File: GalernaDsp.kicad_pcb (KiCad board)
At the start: 4 copper layers, 121 x 121 mm, 124 parts, among them CN100 HX JN1.27-2X5 TP H4.9, J100 DM3CS-SF, J200 Headphones, J201 AudioInput, J202 AudioOutput, J300 USB_C_Receptacle_USB2.0_16P, SW400 100SP1T1B4M2QE, SW401 100SP1T1B4M2QE, U100 SW_RUN, U101 STM32F405RGTx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

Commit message: routing update
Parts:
- C116: footprint Capacitor_SMD:C_0402_1005Metric -> Capacitor_SMD:C_0603_1608Metric
- L100: footprint Inductor_SMD:L_0603_1608Metric -> Inductor_SMD:L_0402_1005Metric
- L300: footprint Inductor_SMD:L_0805_2012Metric -> Inductor_SMD:L_Sunlord_MWSA0618S
- moved R208 36.5 mm to (221.3, 88.4), turned to -90 degrees
- moved R209 35.0 mm to (218.9, 88.4), turned to -90 degrees
- moved C214 32.7 mm to (222.6, 92.5), turned to -90 degrees
- moved R206 32.1 mm to (220.8, 91.7), turned to 90 degrees
- moved R207 31.3 mm to (219.6, 91.7), turned to 90 degrees
- moved C215 29.1 mm to (217.8, 92.5), turned to -90 degrees
- moved FB100 19.1 mm to (223.5, 44.0)
- moved C208 17.9 mm to (201.1, 86.0), turned to 180 degrees
- moved C206 15.8 mm to (201.7, 87.4), turned to 180 degrees
- moved C201 14.8 mm to (211.7, 87.5), turned to 0 degrees
- moved D300 13.7 mm to (234.5, 59.6)
- moved C115 13.7 mm to (223.0, 48.6)
- moved C203 13.2 mm to (205.4, 87.4), turned to 180 degrees
- moved R304 10.7 mm to (234.5, 60.9), turned to 180 degrees
- moved R210 9.41 mm to (224.0, 100.9), turned to 90 degrees
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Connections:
- net /[1] MCU/SWDCLK renamed /[1] MCU/SWD_CLK
- net /[1] MCU/SWDIO renamed /[1] MCU/SWD_IO
- net /[1] MCU/SWO renamed /[1] MCU/SWD_O
- net Net-(U101-VDDA) renamed /[1] MCU/VDDA
- J300 pad S1: GND -> unconnected-(J300-SHIELD-PadS1)_2
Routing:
- net /[1] MCU/OLED_SPI_DATA: track 0.00 -> 104.7 mm
- net /[1] MCU/OLED_SPI_SCK: track 0.00 -> 80.2 mm
- net /[1] MCU/OLED_DC: track 0.00 -> 76.7 mm, vias 0 -> 2
- net /[1] MCU/OLED_RST: track 0.00 -> 72.2 mm, vias 0 -> 2
- net /[1] MCU/OLED_SPI_CS: track 0.00 -> 61.0 mm
- net GND: track 2.08 -> 49.1 mm, vias 0 -> 49
- net /[1] MCU/MCU_NRST: track 0.00 -> 41.3 mm, vias 0 -> 2
- net CODEC_I2S_MCK: track 0.00 -> 35.5 mm
- net CODEC_I2S_SDI: track 0.00 -> 32.5 mm, vias 0 -> 2
- net CODEC_I2C_SCL: track 0.00 -> 29.2 mm, vias 0 -> 2
- net MCU_USB_D-: track 0.00 -> 27.6 mm
- net MCU_USB_D+: track 0.00 -> 27.6 mm
- net CODEC_I2S_SD: track 0.00 -> 27.3 mm
- net CODEC_I2C_SDA: track 0.00 -> 26.5 mm
- net /[1] MCU/SWD_IO: track 0.00 -> 25.2 mm
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- added copper zone on F.Cu, net +3V3A
- added copper zone on F.Cu, net /[1] MCU/VDDA
- added copper zone on F.Cu, net /[2] Power/BUCK_SW
- added copper zone on F.Cu, net VBUS
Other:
- board text added: "PWR_ON"

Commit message: last updates
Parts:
- moved C115 8.18 mm to (231.2, 48.5), turned to 180 degrees
- moved FB100 7.74 mm to (221.6, 36.5)
- moved R105 6.78 mm to (206.1, 54.6)
- moved C113 5.69 mm to (213.7, 35.5)
- moved C111 3.00 mm to (213.8, 36.9)
- moved R110 2.43 mm to (175.8, 87.9)
- moved R112 2.40 mm to (181.5, 87.9)
- moved D101 2.40 mm to (175.8, 91.3)
- moved D102 2.38 mm to (178.6, 91.3)
- moved D103 2.38 mm to (181.5, 91.3)
- moved R111 2.34 mm to (178.6, 87.9)
- moved R109 1.89 mm to (211.4, 54.6)
- moved D104 1.78 mm to (210.9, 36.2)
- moved R106 1.55 mm to (214.4, 54.6)
- moved R108 1.55 mm to (208.3, 54.6)
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- renumbered CN100 to SWD
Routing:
- net Net-(J100-CLK): track 0.00 -> 31.3 mm
- net /[1] MCU/SDCARD_SDIO_D0: track 0.00 -> 28.6 mm, vias 0 -> 2
- net /[1] MCU/SDCARD_SDIO_D1: track 0.00 -> 25.9 mm, vias 0 -> 2
- net /[1] MCU/SDCARD_SDIO_D3: track 0.00 -> 21.6 mm
- net /[1] MCU/SDCARD_DETECT: track 0.00 -> 18.7 mm
- net /[1] MCU/SDCARD_SDIO_CMD: track 0.00 -> 17.9 mm, vias 0 -> 2
- net /[1] MCU/SDCARD_SDIO_D2: track 0.00 -> 15.8 mm
- net /[1] MCU/MCU_NRST: track 41.3 -> 35.2 mm
- net /[1] MCU/SDCARD_SDIO_CK: track 0.00 -> 2.54 mm
- net /[1] MCU/SWD_CLK: track 12.5 -> 14.1 mm, vias 0 -> 2
- net /[1] MCU/SWD_IO: track 25.2 -> 25.1 mm, vias 0 -> 2
- net GND: vias 49 -> 59

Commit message: updated placement
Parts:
- moved FB100 12.0 mm to (230.0, 45.0)
- moved C115 7.41 mm to (234.2, 55.3)
- moved D104 2.77 mm to (213.6, 36.8)
- moved C113 2.73 mm to (211.0, 35.4)
- moved C111 2.21 mm to (211.6, 36.8)
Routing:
- net /[1] MCU/SDCARD_SDIO_CMD: track 17.9 -> 37.6 mm, vias 2 -> 4
- net /[1] MCU/SDCARD_SDIO_D2: track 15.8 -> 31.8 mm, vias 0 -> 2
- net /[1] MCU/SDCARD_SDIO_D3: track 21.6 -> 37.5 mm, vias 0 -> 2
- net /[1] MCU/SDCARD_SDIO_D1: track 25.9 -> 41.8 mm
- net /[1] MCU/SDCARD_SDIO_D0: track 28.6 -> 44.3 mm, vias 2 -> 4
- net Net-(J100-CLK): track 31.3 -> 33.9 mm, vias 0 -> 2
- net GND: track 49.1 -> 50.7 mm, vias 59 -> 74
- added copper zone on F.Cu, net /[1] MCU/+3V3_SD

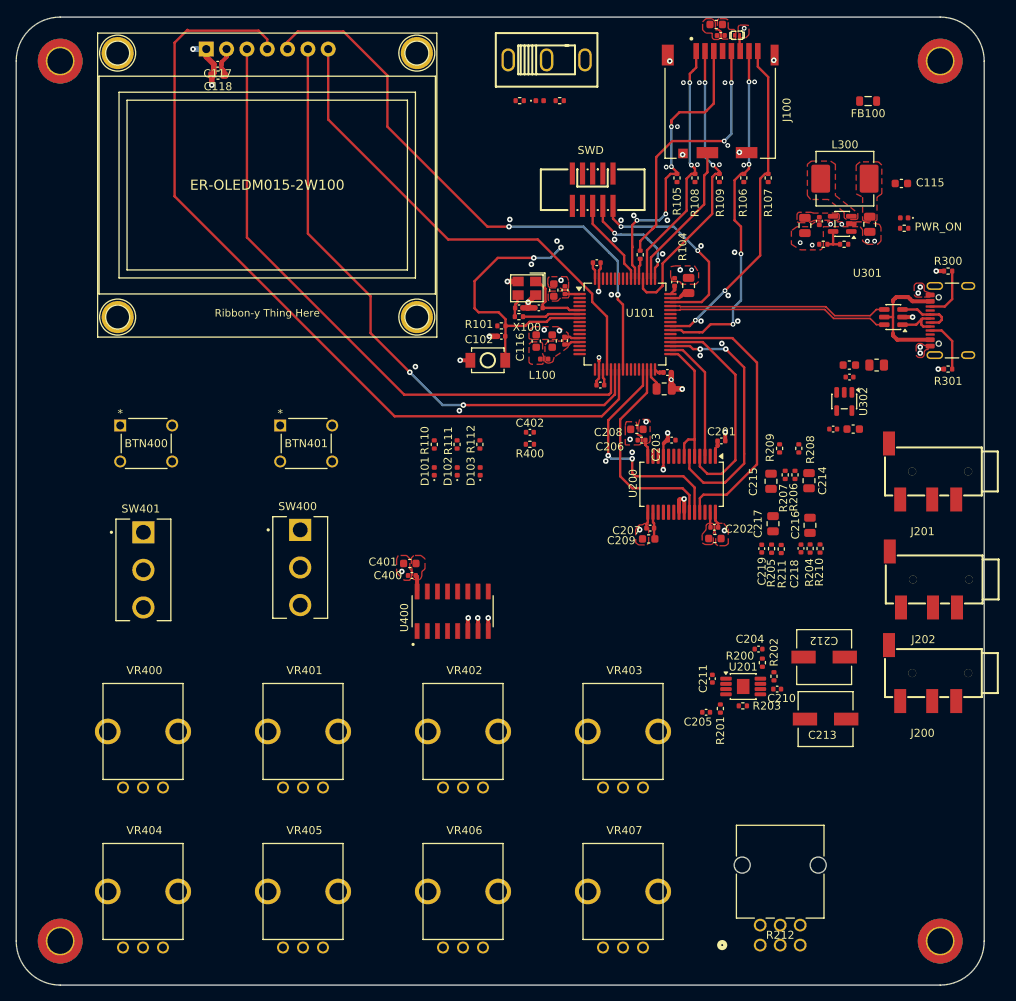
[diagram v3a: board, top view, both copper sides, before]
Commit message: headphone amplifier routing
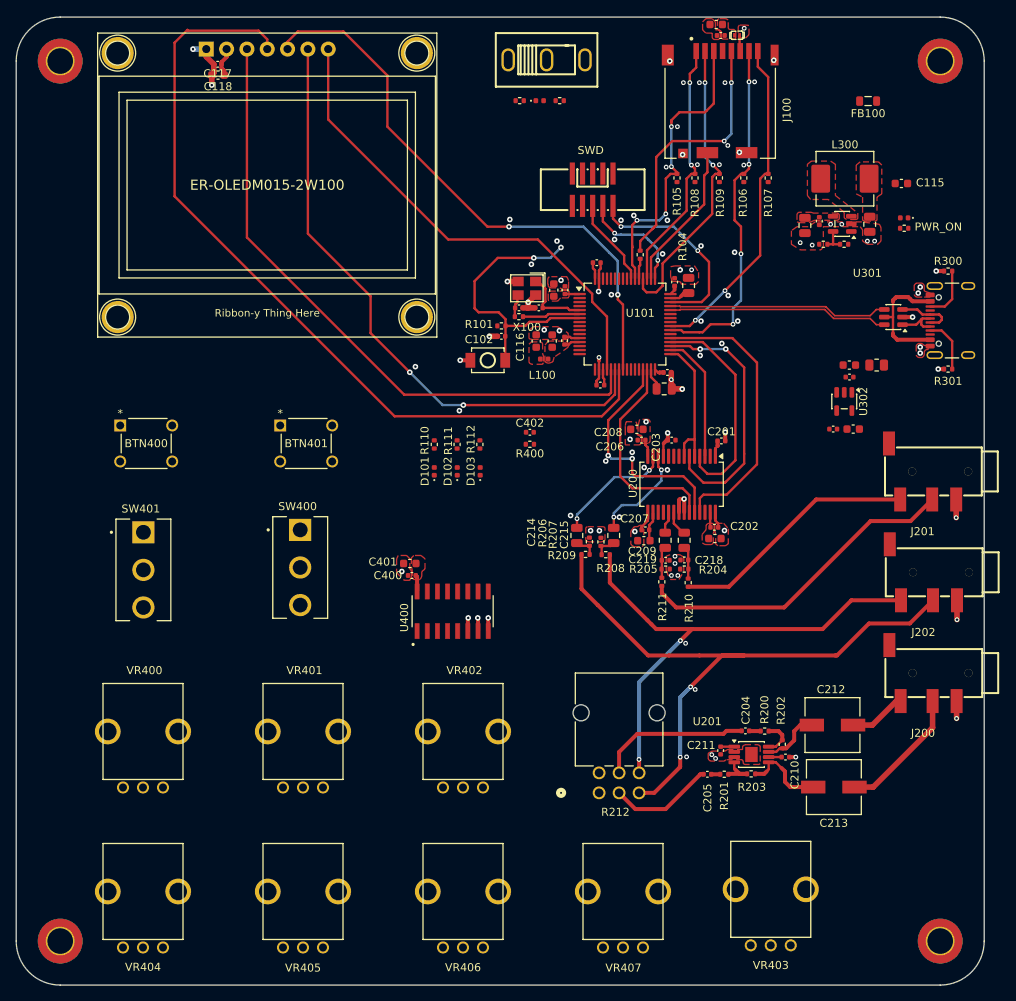
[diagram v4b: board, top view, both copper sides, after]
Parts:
- moved R212 27.7 mm to (196.4, 131.5)
- moved R209 27.6 mm to (194.7, 101.7), turned to 180 degrees
- moved R208 27.5 mm to (197.2, 101.7), turned to 0 degrees
- moved VR403 27.0 mm to (217.8, 150.5)
- moved R207 25.9 mm to (195.2, 100.1), turned to -90 degrees
- moved R206 25.7 mm to (196.6, 100.1), turned to -90 degrees
- moved C214 25.4 mm to (198.2, 99.3), turned to 90 degrees
- moved C215 25.2 mm to (193.6, 99.3), turned to 90 degrees
- moved R210 17.0 mm to (207.5, 105.2)
- moved R204 15.9 mm to (207.0, 103.5), turned to 0 degrees
- moved C216 15.8 mm to (207.0, 99.9), turned to 90 degrees
- moved R211 15.5 mm to (204.2, 105.1)
- moved C218 14.7 mm to (207.0, 102.4), turned to 180 degrees
- moved C217 13.6 mm to (204.6, 99.9), turned to 90 degrees
- moved R205 13.5 mm to (204.7, 103.5), turned to 180 degrees
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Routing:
- net /[2] Audio/AUDIO_R_OUT: track 0.00 -> 79.9 mm, vias 0 -> 2
- net /[2] Audio/AUDIO_L_OUT: track 0.00 -> 64.5 mm, vias 0 -> 2
- net /[2] Audio/AUDIO_R_IN: track 0.00 -> 41.0 mm
- net /[2] Audio/AUDIO_L_IN: track 0.00 -> 31.0 mm
- net /[2] Audio/AUDIO_WIPER_OUT_L: track 0.00 -> 19.0 mm
- net /[2] Audio/HEADPHONE_OUT_R: track 0.00 -> 16.2 mm
- net /[2] Audio/CODEC_R_OUT: track 0.00 -> 14.9 mm, vias 0 -> 2
- net /[2] Audio/AUDIO_WIPER_OUT_R: track 0.00 -> 13.2 mm
- net /[2] Audio/CODEC_L_OUT: track 0.00 -> 12.7 mm, vias 0 -> 2
- net Net-(U201-VO2): track 0.00 -> 10.4 mm
- net Net-(U201-VO1): track 0.00 -> 7.46 mm
- net /[2] Audio/HEADPHONE_OUT_L: track 0.00 -> 7.18 mm
- net GND: track 50.7 -> 57.1 mm, vias 74 -> 92
- net Net-(U201-IN2-): track 0.00 -> 5.09 mm
- net Net-(U201-IN1-): track 0.00 -> 4.58 mm
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
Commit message: pcb updated
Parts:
- moved D300 5.82 mm to (240.2, 58.5)
- moved R304 5.82 mm to (240.2, 59.8)
- moved C303 5.63 mm to (231.1, 82.5), turned to -90 degrees
- moved C305 5.46 mm to (223.3, 83.5)
- moved D100 4.78 mm to (184.2, 44.1)
- moved R100 4.78 mm to (181.7, 44.1)
- moved R102 4.78 mm to (186.7, 44.1)
- moved C304 4.77 mm to (223.8, 81.6), turned to 180 degrees
- moved C300 3.87 mm to (226.6, 57.2)
- moved C306 3.87 mm to (232.9, 57.6)
- moved R303 3.87 mm to (227.1, 60.1)
- moved U301 3.87 mm to (229.4, 57.6)
- moved C302 3.87 mm to (224.8, 57.8)
- moved L300 3.87 mm to (229.8, 51.9)
- moved R302 3.87 mm to (229.7, 60.1)
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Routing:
- net +3V3A: track 3.77 -> 75.3 mm, vias 1 -> 6
- net /[1] MCU/MCU_BOOT0: track 0.00 -> 30.2 mm, vias 0 -> 2
- net VBUS: track 15.6 -> 43.3 mm
- net GND: track 57.1 -> 83.3 mm, vias 92 -> 106
- net /[1] MCU/+3V3_SD: track 0.00 -> 22.8 mm
- net +3V3: track 18.1 -> 33.3 mm, vias 0 -> 2
- net PUSH_BTN_0: track 0.00 -> 6.50 mm
- net Net-(D100-A): track 0.00 -> 6.23 mm
- net /[1] MCU/MCU_NRST: track 35.2 -> 41.0 mm
- net /[2] Power/LDO_IN: track 0.00 -> 5.72 mm
- net /[2] Power/LDO_BP: track 0.00 -> 1.61 mm
- net Net-(D100-K): track 0.00 -> 1.50 mm
- net Net-(D300-K): track 0.00 -> 1.31 mm
- net Net-(U201-VO2): track 10.4 -> 9.66 mm
- added copper zone on F.Cu, net /[2] Power/LDO_IN
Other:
- board text added: "PWR"
- board text removed: "PWR_ON"

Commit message: last update
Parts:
- moved C109 0.68 mm to (208.2, 68.2)
- moved C107 0.58 mm to (204.5, 81.5)
- moved C106 0.55 mm to (204.5, 79.3), turned to -90 degrees
- moved SW401 0.30 mm to (139.4, 103.3)
- moved C108 0.25 mm to (206.0, 67.7), turned to 0 degrees
- renumbered SWD to CN100
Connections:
- U101 pad 26: POT_MUX_SEL_2 -> POT_MUX_SEL_0
- U101 pad 28: POT_MUX_SEL_0 -> POT_MUX_SEL_2
- U101 pad 8: SW_0 -> SW_1
- U101 pad 9: SW_1 -> SW_0
- U400 pad 13: /[3] Input Control/POT_0_CTL -> /[3] Input Control/POT_1_CTL
- U400 pad 14: /[3] Input Control/POT_1_CTL -> /[3] Input Control/POT_2_CTL
- U400 pad 15: /[3] Input Control/POT_2_CTL -> /[3] Input Control/POT_0_CTL
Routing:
- net +3V3: track 33.3 -> 521.6 mm, vias 2 -> 27
- net /[3] Input Control/POT_2_CTL: track 0.00 -> 81.7 mm, vias 0 -> 2
- net SW_1: track 0.00 -> 77.5 mm, vias 0 -> 2
- net /[3] Input Control/POT_5_CTL: track 0.00 -> 73.2 mm
- net /[3] Input Control/POT_7_CTL: track 0.00 -> 59.0 mm
- net SW_0: track 0.00 -> 56.4 mm, vias 0 -> 2
- net /[3] Input Control/POT_0_CTL: track 0.00 -> 53.2 mm
- net /[3] Input Control/POT_3_CTL: track 0.00 -> 52.7 mm, vias 0 -> 2
- net /[3] Input Control/POT_6_CTL: track 0.00 -> 46.0 mm
- net POT_MUX_SEL_0: track 0.00 -> 36.3 mm, vias 0 -> 2
- net POT_MUX_SEL_1: track 0.00 -> 35.9 mm, vias 0 -> 2
- net POT_MUX_SEL_2: track 0.00 -> 35.6 mm, vias 0 -> 2
- net GND: track 83.3 -> 117.8 mm, vias 106 -> 137
- net Net-(U400-COM_OUT/IN): track 0.00 -> 31.4 mm
- net /[3] Input Control/POT_4_CTL: track 0.00 -> 28.8 mm
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
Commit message: last status
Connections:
- U101 pad 56: PUSH_BTN_0 -> SW_0
- U101 pad 57: PUSH_BTN_1 -> SW_1
- U101 pad 8: SW_1 -> PUSH_BTN_1
- U101 pad 9: SW_0 -> PUSH_BTN_0
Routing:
- net PUSH_BTN_0: track 6.50 -> 78.3 mm, vias 0 -> 2
- net PUSH_BTN_1: track 6.50 -> 60.0 mm, vias 0 -> 2
- net GND: track 117.8 -> 87.1 mm, vias 137 -> 126
- net SW_0: track 56.4 -> 64.9 mm
- net SW_1: track 77.5 -> 83.5 mm
- net +3V3: track 521.6 -> 518.9 mm, vias 27 -> 28
- net /[1] MCU/+3V3_SD: track 22.8 -> 24.8 mm

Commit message: Fixing main DRC on pcb
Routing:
- net +3V3: track 518.9 -> 550.2 mm, vias 28 -> 30
- net VBUS: track 43.3 -> 55.4 mm
- net POT_MUX_SEL_0: track 36.3 -> 36.9 mm
- net /[1] MCU/OLED_SPI_CS: track 61.0 -> 61.5 mm
- net GND: track 87.1 -> 87.5 mm, vias 126 -> 130
